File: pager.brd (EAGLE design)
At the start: 78.4 x 44.8 mm, 66 parts, among them Q1 25 MHz, Q2 SI2333DS, SW1 CHS-01A1, SW2 CHS-01A1, U1 VOCORE2-SMD, U2 VOCORE2-SMD, U3 XR22800IL, U4 IP4234CZ6, X1 OMRON_XF2L-30REVERSE, X2 FCI_8193_MICRO_USB

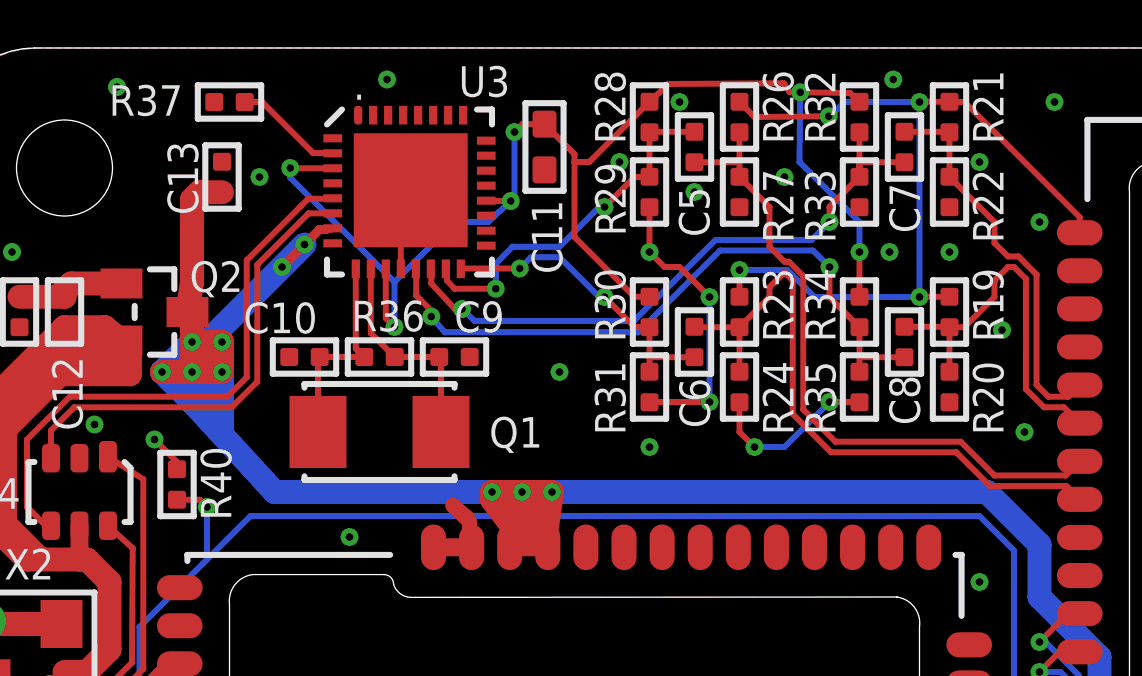
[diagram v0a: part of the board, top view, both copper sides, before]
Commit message: even thicker power bus
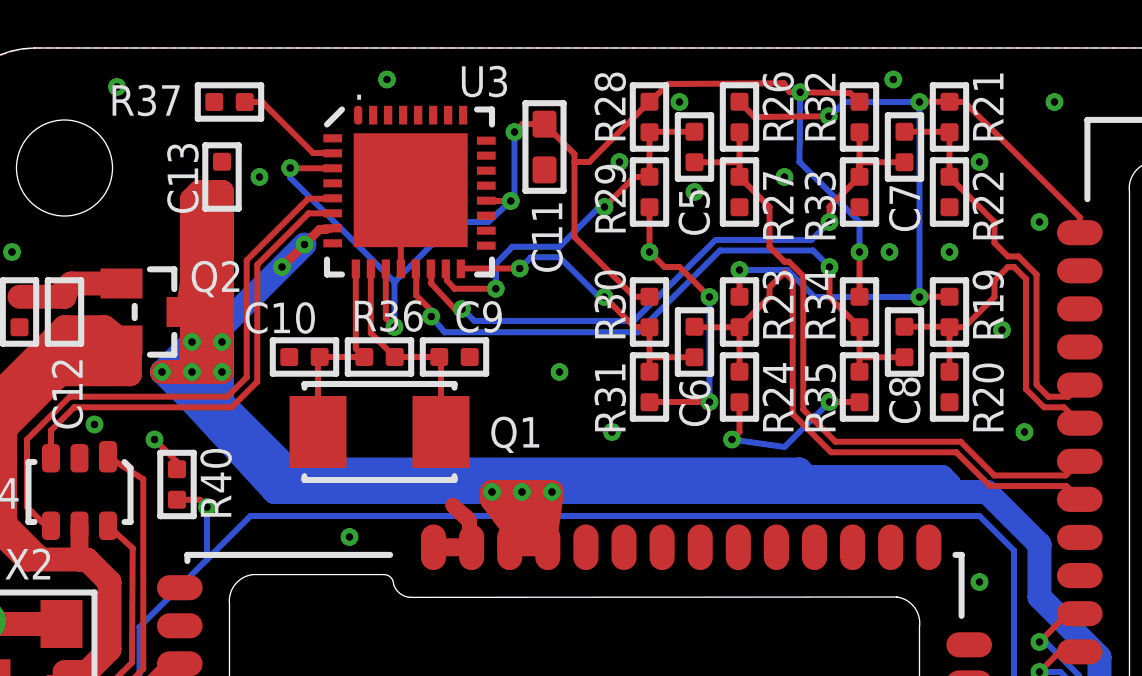
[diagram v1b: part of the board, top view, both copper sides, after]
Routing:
- net +5V: track 132.6 -> 173.5 mm
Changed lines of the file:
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@@
 <wire x1="8.25" y1="34" x2="8.75" y2="34" width="0.8" layer="16"/>
 <wire x1="8.75" y1="34" x2="8.75" y2="35" width="0.8" layer="16"/>
-<wire x1="9.25" y1="34" x2="9.25" y2="33" width="0.8" layer="16"/>
 <wire x1="9.25" y1="32" x2="9.25" y2="33" width="0.8" layer="16"/>
 <wire x1="9.25" y1="33" x2="8.75" y2="33" width="0.8" layer="16"/>
 <wire x1="8.75" y1="33" x2="8.75" y2="33.5" width="0.8" layer="16"/>
 <wire x1="12" y1="38.25" x2="8.75" y2="35" width="0.8" layer="16"/>
+<wire x1="8.25" y1="36" x2="9.25" y2="35" width="0.8" layer="1"/>
+<wire x1="9.25" y1="35" x2="9.25" y2="40" width="0.8" layer="1"/>
+<wire x1="9.25" y1="40" x2="9" y2="40" width="0.8" layer="1"/>
+<wire x1="9" y1="40" x2="8.75" y2="39.75" width="0.8" layer="1"/>
+<wire x1="8.75" y1="39.75" x2="8.75" y2="36" width="0.8" layer="1"/>
+<wire x1="9.25" y1="34" x2="9.25" y2="33" width="0.8" layer="16"/>
+<wire x1="9.25" y1="33" x2="11.5" y2="30.75" width="0.8" layer="16"/>
+<wire x1="11.5" y1="30.75" x2="28.5" y2="30.75" width="0.8" layer="16"/>
+<wire x1="28.5" y1="30.75" x2="28.75" y2="30.5" width="0.8" layer="16"/>
+<wire x1="28.75" y1="30.5" x2="33.25" y2="30.5" width="0.8" layer="16"/>
+<wire x1="33.25" y1="30.5" x2="33.5" y2="30.25" width="0.8" layer="16"/>
+<wire x1="8.25" y1="34" x2="8.25" y2="33.5" width="0.8" layer="16"/>
+<wire x1="8.25" y1="33.5" x2="11.25" y2="30.5" width="0.8" layer="16"/>
 </signal>
 <signal name="GND" class="3">
@@
 <wire x1="23.508" y1="33" x2="23.5" y2="32.992" width="0.2" layer="1"/>
 <wire x1="26.5" y1="32.992" x2="26.5" y2="32" width="0.2" layer="1"/>
-<wire x1="26.5" y1="32" x2="27" y2="31.5" width="0.2" layer="1"/>
-<via x="27" y="31.5" extent="1-16" drill="0.25" diameter="0.6"/>
-<wire x1="27" y1="31.5" x2="28" y2="31.5" width="0.2" layer="16"/>
+<wire x1="26.5" y1="32" x2="26.25" y2="31.75" width="0.2" layer="1"/>
+<via x="26.25" y="31.75" extent="1-16" drill="0.25" diameter="0.6"/>
+<wire x1="26.25" y1="31.75" x2="28" y2="31.5" width="0.2" layer="16"/>
 <wire x1="28" y1="31.5" x2="29.5" y2="33" width="0.2" layer="16"/>
 <via x="29.5" y="33" extent="1-16" drill="0.25" diameter="0.6"/>
@@
 <via x="28" y="40.5" extent="1-16" drill="0.25" diameter="0.6"/>
 <via x="31.625" y="43.75" extent="1-16" drill="0.25" diameter="0.6"/>
-<via x="23.5" y="31.5" extent="1-16" drill="0.25" diameter="0.6"/>
+<via x="22.25" y="32" extent="1-16" drill="0.25" diameter="0.6"/>
 <via x="49" y="10.5" extent="1-16" drill="0.25" diameter="0.6"/>
 <via x="46.3" y="12.725" extent="1-16" drill="0.25" diameter="0.6"/>

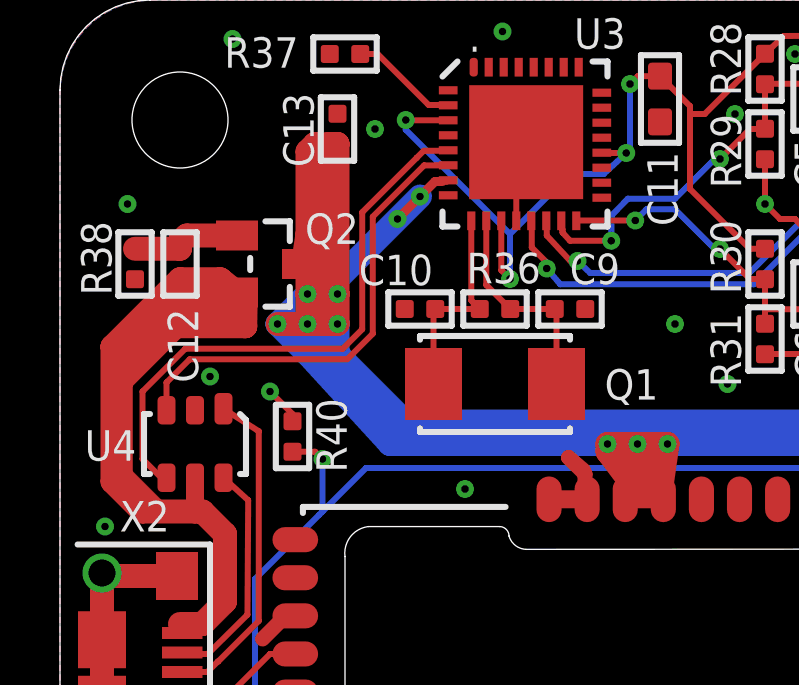
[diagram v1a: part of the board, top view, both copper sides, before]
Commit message: a few extra ground-plane vias
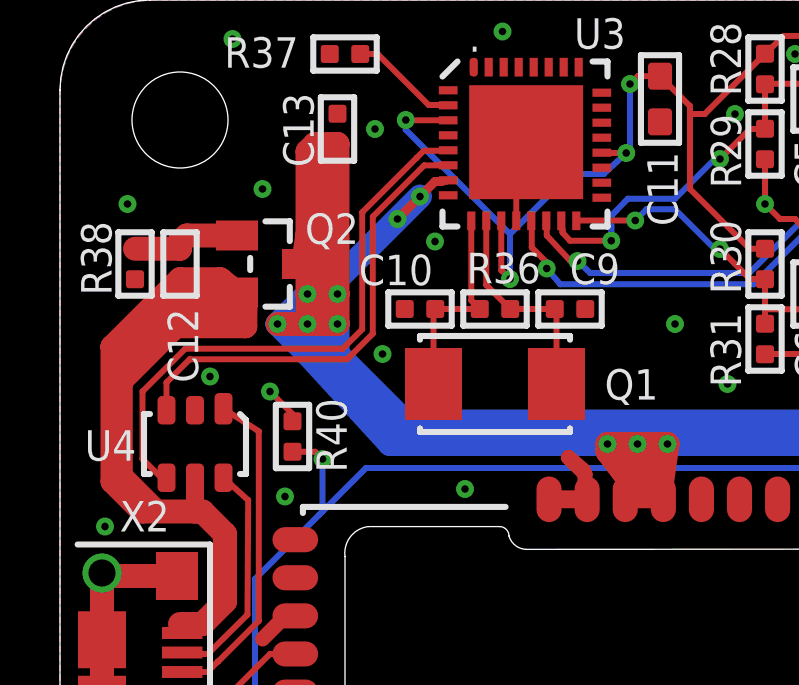
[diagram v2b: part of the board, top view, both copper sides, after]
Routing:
- net GND: vias 79 -> 83
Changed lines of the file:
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@@
 <wire x1="7.75" y1="30.758" x2="7.75" y2="31" width="0.2" layer="1"/>
 <wire x1="7.75" y1="31" x2="7" y2="31.75" width="0.2" layer="1"/>
+<via x="10.75" y="33" extent="1-16" drill="0.25" diameter="0.6"/>
+<via x="12.5" y="36.75" extent="1-16" drill="0.25" diameter="0.6"/>
+<via x="6.75" y="38.5" extent="1-16" drill="0.25" diameter="0.6"/>
+<via x="7.5" y="28.25" extent="1-16" drill="0.25" diameter="0.6"/>
 </signal>
 <signal name="ETH_1B_TX_P" class="1">

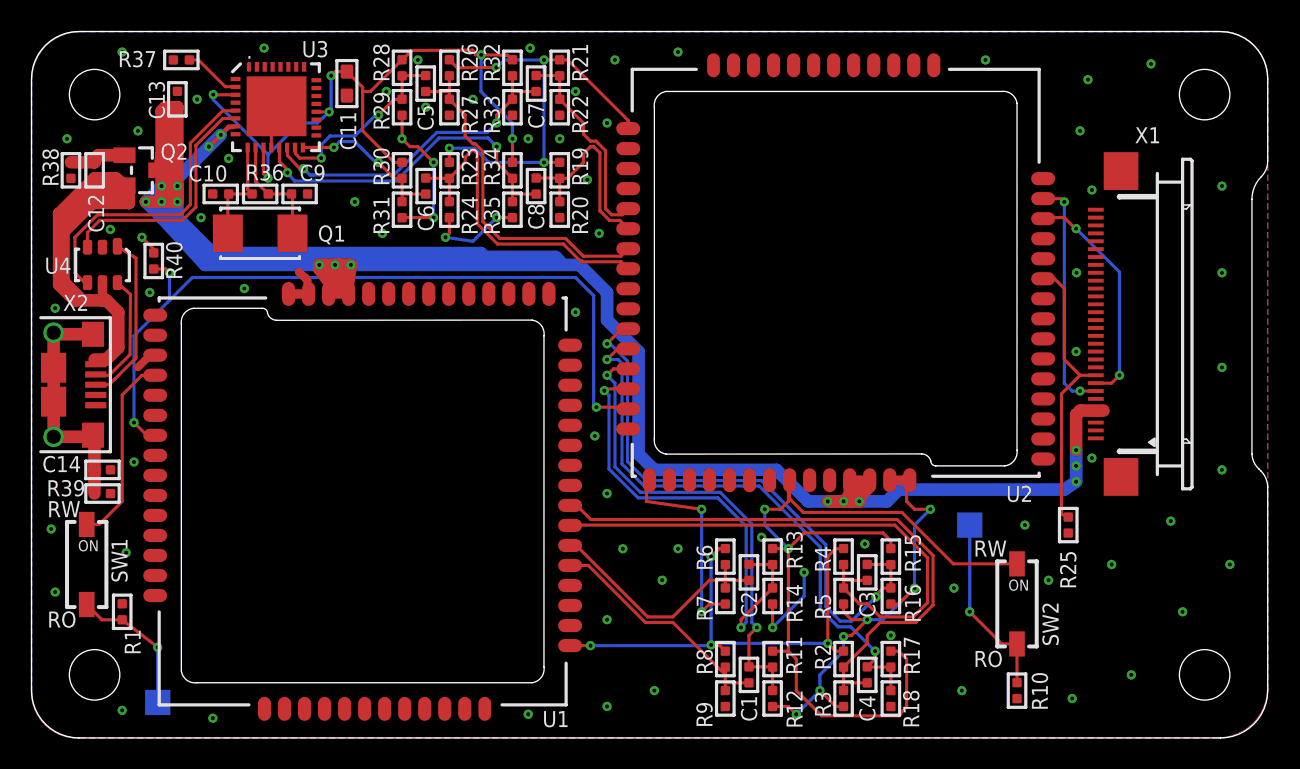
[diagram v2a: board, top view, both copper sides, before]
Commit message: added SD-card
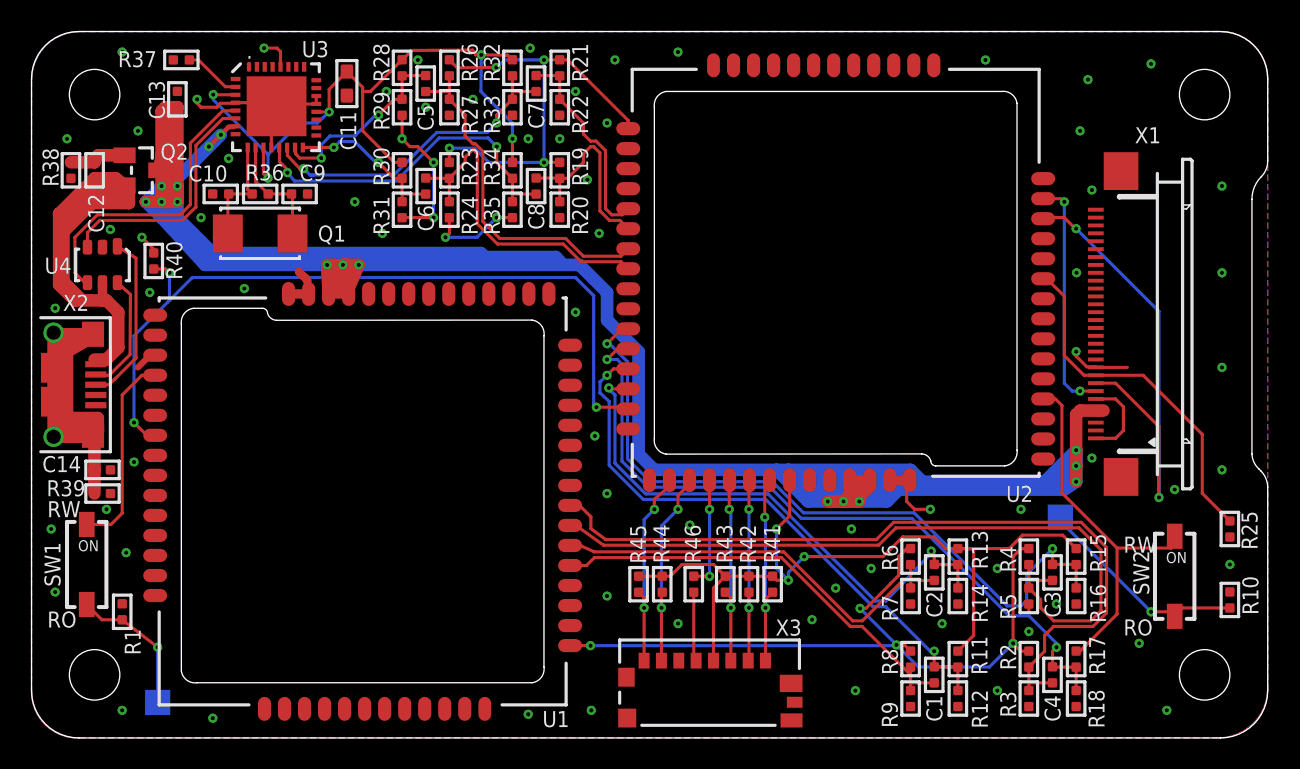
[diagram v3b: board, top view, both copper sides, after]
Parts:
- added R41, R42, R43, R44, R45: 10k, pager:_0402
- added R46: 22, pager:_0402
- added X3: MOLEX_475710001_MICROSD_SOCKET, pager:MOLEX_475710001_MICROSD_SOCKET
- moved R10 14.7 mm to (76.0, 8.75), turned to 270 degrees
- moved C1 11.8 mm to (57.2, 4.00)
- moved C2 11.8 mm to (57.2, 10.5)
- moved C3 11.8 mm to (64.8, 10.5)
- moved C4 11.8 mm to (64.8, 4.00)
- moved R11 11.8 mm to (58.8, 5.00)
- moved R12 11.8 mm to (58.8, 2.50)
- moved R13 11.8 mm to (58.8, 11.5)
- moved R14 11.8 mm to (58.8, 9.00)
- moved R15 11.8 mm to (66.2, 11.5)
- moved R16 11.8 mm to (66.2, 9.00)
- moved R17 11.8 mm to (66.2, 5.00)
- moved R18 11.8 mm to (66.2, 2.50)
- moved R2 11.8 mm to (63.2, 5.00)
- moved R3 11.8 mm to (63.2, 2.50)
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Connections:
- new net N$2: R46.1, X3.P5
- new net SD_CLK: R46.2, U2.PB03
- new net SD_CMD: R43.1, U2.PB04, X3.P3
- new net SD_D0: R44.1, U2.PB02, X3.P7
- new net SD_D1: R45.1, U2.PB01, X3.P8
- new net SD_D2: R41.1, U2.PB06, X3.P1
- new net SD_D3: R42.1, U2.PB05, X3.P2
- net 3.3_CORE: now also R41.2, R42.2, R43.2, R44.2, R45.2, X3.P4
- net GND: now also X3.G1, X3.G2, X3.G3, X3.P6
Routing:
- net +5V: track 173.5 -> 220.1 mm
- net GND: track 73.0 -> 49.1 mm, vias 83 -> 75
- net 3.3_CORE: track 83.4 -> 104.0 mm, vias 6 -> 7
- net SHIELD: track 15.4 -> 34.6 mm
- net DISP_RX0: track 14.6 -> 31.3 mm
- net 3.3_WIFI: track 44.3 -> 59.9 mm
- net SD_D1: track 0.00 -> 13.3 mm, vias 0 -> 2
- net SD_D0: track 0.00 -> 13.2 mm, vias 0 -> 2
- net SD_D2: track 0.00 -> 12.8 mm, vias 0 -> 2
- net SD_CMD: track 0.00 -> 12.6 mm, vias 0 -> 2
- net SD_D3: track 0.00 -> 12.5 mm, vias 0 -> 2
- net ETH_2B_TX_N: track 38.1 -> 50.5 mm
- net ETH_2B_RX_P: track 15.7 -> 27.9 mm
- net ETH_2B_TX_P: track 36.3 -> 48.4 mm
- net ETH_2B_RX_N: track 16.1 -> 28.0 mm
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
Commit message: minor silkscreen fixes
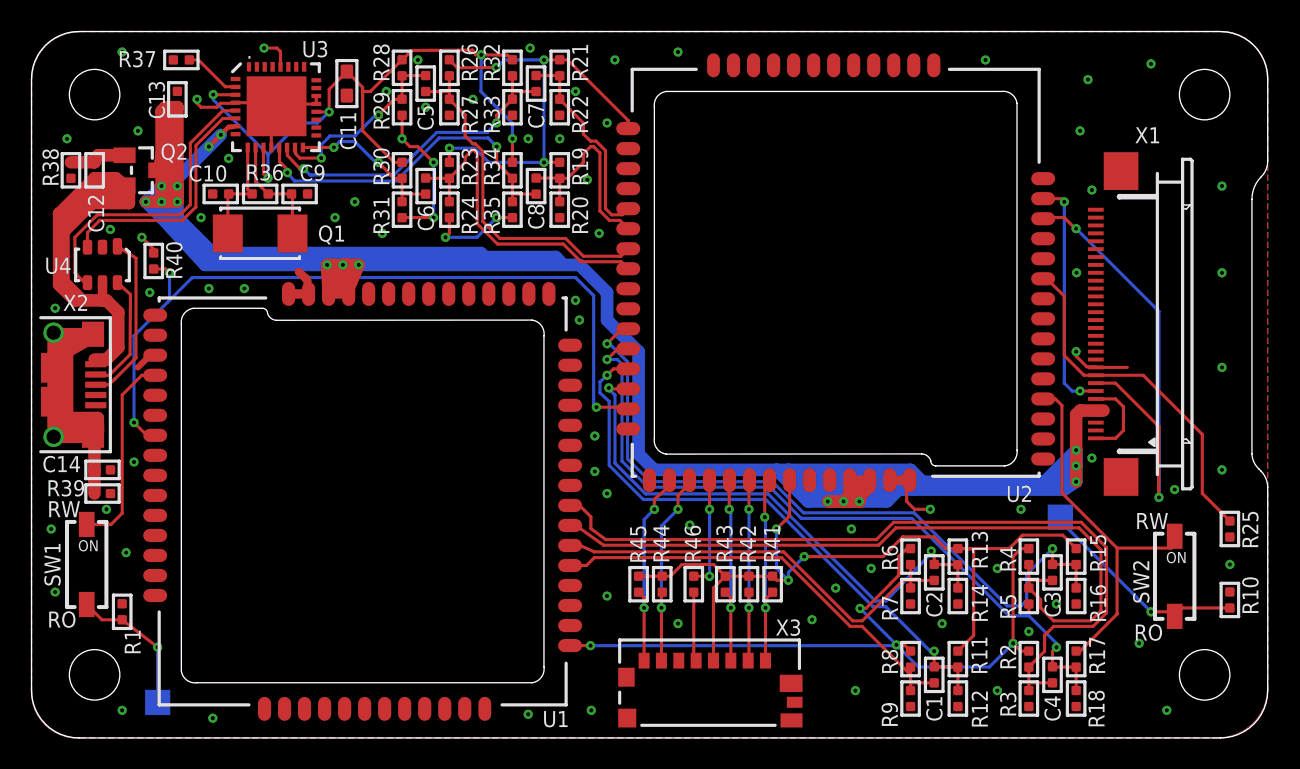
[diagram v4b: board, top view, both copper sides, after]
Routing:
- net GND: vias 75 -> 79
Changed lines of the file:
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@@
 <hole x="74.4" y="4" drill="3.2"/>
 <text x="1" y="14" size="1.016" layer="21" font="vector" ratio="14">RW</text>
-<text x="69.25" y="11.75" size="1.016" layer="21" font="vector" ratio="14">RW</text>
+<text x="70" y="13.25" size="1.016" layer="21" font="vector" ratio="14">RW</text>
 <text x="1" y="7" size="1.016" layer="21" font="vector" ratio="14">RO</text>
-<text x="69.25" y="6.5" size="1.016" layer="21" font="vector" ratio="14">RO</text>
+<text x="69.9125" y="6.175" size="1.016" layer="21" font="vector" ratio="14">RO</text>
 </plain>
 <attributes>
@@
 </element>
 <element name="R25" library="pager" package="_0402" value="10 k" x="76" y="13.25" smashed="yes" rot="R90">
-<attribute name="NAME" x="77.7561" y="11.93" size="1.016" layer="25" font="vector" ratio="14" rot="R90"/>
+<attribute name="NAME" x="77.8061" y="11.98" size="1.016" layer="25" font="vector" ratio="14" rot="R90"/>
 <attribute name="VALUE" x="77.3336" y="11.98" size="0.508" layer="27" font="vector" ratio="10" rot="R90"/>
 </element>
@@
 </element>
 <element name="SW2" library="pager" package="CHS-01A1" value="CHS-01A1" x="72.5" y="10.25" smashed="yes">
-<attribute name="NAME" x="70.8878" y="9.0608" size="1.016" layer="25" font="vector" ratio="14" rot="R90"/>
+<attribute name="NAME" x="70.8878" y="8.4983" size="1.016" layer="25" font="vector" ratio="14" rot="R90"/>
 </element>
 <element name="U4" library="pager" package="TSOP-6" value="IP4234CZ6" x="4.5" y="30" smashed="yes" rot="R180">
@@
 <via x="13.5" y="28.5" extent="1-16" drill="0.25" diameter="0.6"/>
 <via x="7" y="31.75" extent="1-16" drill="0.25" diameter="0.6"/>
-<via x="34.5" y="27" extent="1-16" drill="0.25" diameter="0.6"/>
+<via x="34.75" y="26.5" extent="1-16" drill="0.25" diameter="0.6"/>
 <via x="36.5" y="39" extent="1-16" drill="0.25" diameter="0.6"/>
 <via x="34.5" y="41" extent="1-16" drill="0.25" diameter="0.6"/>
@@
 <wire x1="69.25" y1="19.5" x2="68.75" y2="19" width="0.2" layer="1"/>
 <wire x1="68.75" y1="19" x2="67.5" y2="19" width="0.2" layer="1"/>
+<via x="34.5" y="27.75" extent="1-16" drill="0.25" diameter="0.6"/>
+<via x="35.725" y="16.9" extent="1-16" drill="0.25" diameter="0.6"/>
+<via x="11.25" y="28.5" extent="1-16" drill="0.25" diameter="0.6"/>
+<via x="19.25" y="33" extent="1-16" drill="0.25" diameter="0.6"/>
 </signal>
 <signal name="ETH_1B_TX_P" class="1">
